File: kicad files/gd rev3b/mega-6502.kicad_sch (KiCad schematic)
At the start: 63 parts, among them J1 XY, Q1 BC817, SW1 MEGA RESET, U1 Apple_MEGA_II, U10 DRAM64KX4, U2 w65c02s, U3 74LVC1G02, U35 74LVC2G04, U4 74HC245, U5 74HC245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

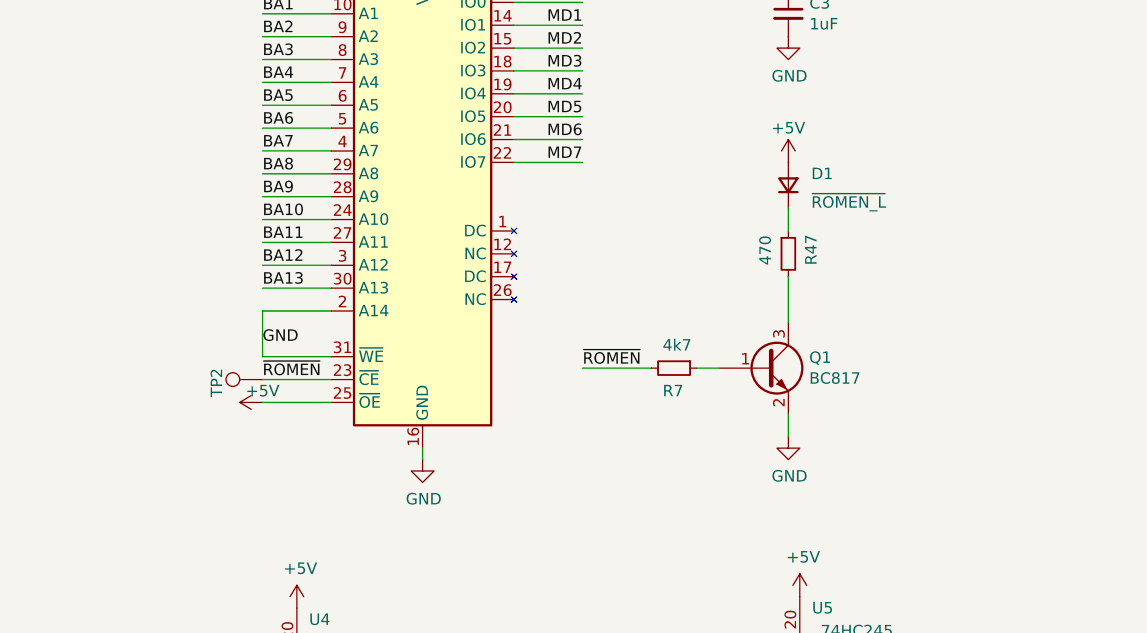
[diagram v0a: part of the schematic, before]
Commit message: Schematic changes for #52, #50, #70, #51, #61, #69, #71
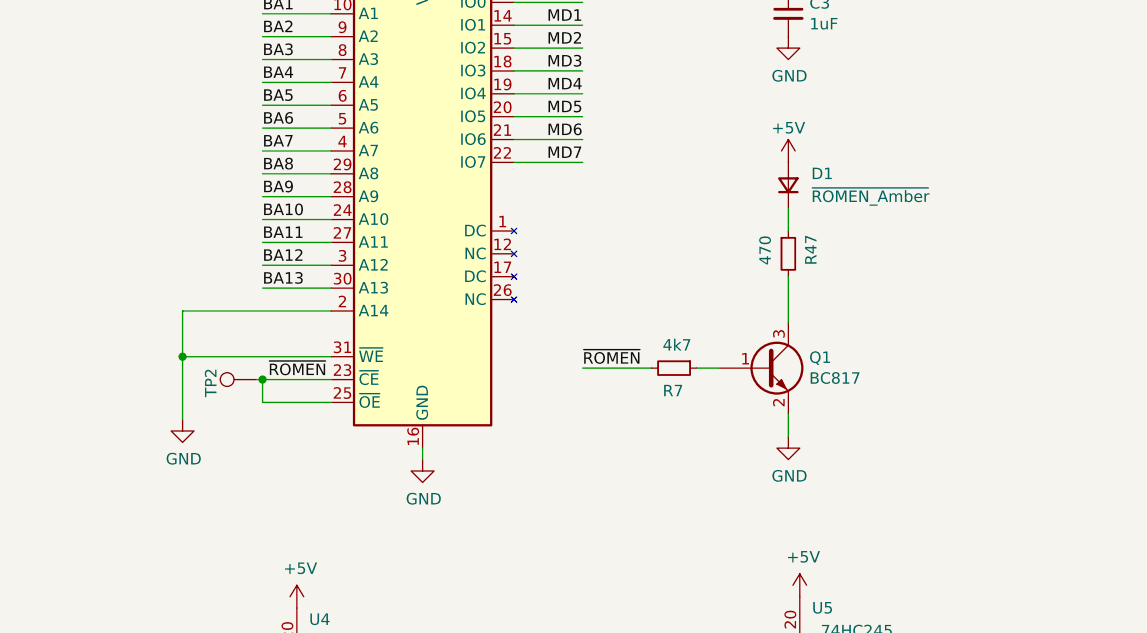
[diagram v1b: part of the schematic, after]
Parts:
- D1: value ~{ROMEN_L} -> ~{ROMEN_Amber}
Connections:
- net +5V: no longer U6.25 (~{OE})
- net ~{ROMEN}: now also U6.25 (~{OE})
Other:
- moved on the sheet: TP2
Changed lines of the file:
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@@
     (company "twitch.tv/baldengineer")
   )
+  (junction (at 214.63 187.96) (diameter 0) (color 0 0 0 0)
+  )
   (junction (at 350.52 194.31) (diameter 0) (color 0 0 0 0)
   )
@@
   (junction (at 127 187.96) (diameter 0) (color 0 0 0 0)
   )
+  (junction (at 205.74 185.42) (diameter 0) (color 0 0 0 0)
+  )
   (junction (at 127 264.16) (diameter 0) (color 0 0 0 0)
   )
@@
     (stroke (width 0) (type default))
   )
+  (wire (pts (xy 214.63 187.96) (xy 214.63 190.5))
+    (stroke (width 0) (type default))
+  )
   (wire (pts (xy 137.16 228.6) (xy 147.32 228.6))
     (stroke (width 0) (type default))
@@
     (stroke (width 0) (type default))
   )
+  (wire (pts (xy 214.63 187.96) (xy 213.995 187.96))
+    (stroke (width 0) (type default))
+  )
   (wire (pts (xy 242.57 161.29) (xy 250.19 161.29))
     (stroke (width 0) (type default))
@@
     (stroke (width 0) (type default))
   )
+  (wire (pts (xy 205.74 180.34) (xy 205.74 185.42))
+    (stroke (width 0) (type default))
+  )
   (wire (pts (xy 109.22 53.34) (xy 104.14 53.34))
     (stroke (width 0) (type default))
@@
     (stroke (width 0) (type default))
   )
+  (wire (pts (xy 205.74 185.42) (xy 205.74 192.405))
+    (stroke (width 0) (type default))
+  )
   (wire (pts (xy 347.98 148.59) (xy 347.98 149.86))
     (stroke (width 0) (type default))
@@
     (stroke (width 0) (type default))
   )
-  (wire (pts (xy 214.63 180.34) (xy 222.25 180.34))
+  (wire (pts (xy 205.74 180.34) (xy 222.25 180.34))
     (stroke (width 0) (type default))
   )
@@
     (stroke (width 0) (type default))
   )
-  (wire (pts (xy 222.25 185.42) (xy 214.63 185.42))
+  (wire (pts (xy 222.25 185.42) (xy 205.74 185.42))
     (stroke (width 0) (type default))
   )
@@
     (stroke (width 0) (type default))
   )
-  (wire (pts (xy 214.63 180.34) (xy 214.63 185.42))
-    (stroke (width 0) (type default))
-  )
   (wire (pts (xy 318.77 100.33) (xy 325.12 100.33))
     (stroke (width 0) (type default))
@@
     (effects (font (size 1.27 1.27)) (justify left bottom))
   )
-  (label "~{ROMEN}" (at 214.63 187.96 0) (fields_autoplaced)
+  (label "~{ROMEN}" (at 215.265 187.96 0) (fields_autoplaced)
     (effects (font (size 1.27 1.27)) (justify left bottom))
   )
@@
     (effects (font (size 1.27 1.27)) (justify right bottom))
   )
-  (label "GND" (at 214.63 184.15 0) (fields_autoplaced)
-    (effects (font (size 1.27 1.27)) (justify left bottom))
-  )
   (label "~{DMA}" (at 158.75 111.76 180) (fields_autoplaced)
     (effects (font (size 1.27 1.27)) (justify right bottom))
@@
     (effects (font (size 1.27 1.27)) (justify right))
   )
+  (symbol (lib_id "power:GND") (at 205.74 192.405 0) (unit 1)
+    (in_bom yes) (on_board yes) (dnp no)
+    (property "Reference" "#PWR022" (at 205.74 198.755 0)
+      (effects (font (size 1.27 1.27)) hide)
+    )
+    (property "Value" "GND" (at 205.867 196.7992 0)
+      (effects (font (size 1.27 1.27)))
+    )
+    (property "Footprint" "" (at 205.74 192.405 0)
+      (effects (font (size 1.27 1.27)) hide)
+    )
+    (property "Datasheet" "" (at 205.74 192.405 0)
+      (effects (font (size 1.27 1.27)) hide)
+    )
+    (pin "1")
+    (instances
+      (project "gd rev3b"
+        (path "/e63e39d7-6ac0-4ffd-8aa3-1841a4541b55/1d17904d-638f-48f3-894f-0144911f4a7c"
+          (reference "#PWR022") (unit 1)
+        )
+      )
+    )
+  )
   (symbol (lib_id "Mega IIe Rev3 Symbols:C_Small") (at 389.89 229.87 0) (unit 1)
     (in_bom yes) (on_board yes) (dnp no)
@@
     )
   )
-  (symbol (lib_name "TestPoint_Harwin_1") (lib_id "Mega IIe Rev3 Symbols:TestPoint_Harwin_1") (at 214.63 187.96 90) (unit 1)
+  (symbol (lib_name "TestPoint_Harwin_1") (lib_id "Mega IIe Rev3 Symbols:TestPoint_Harwin_1") (at 213.995 187.96 90) (unit 1)
     (in_bom yes) (on_board yes) (dnp no)
-    (property "Reference" "TP2" (at 209.55 186.69 0)
+    (property "Reference" "TP2" (at 208.915 186.69 0)
       (effects (font (size 1.27 1.27)) (justify right))
     )
-    (property "Value" "TestPoint_Harwin" (at 213.9442 186.4868 0)
+    (property "Value" "TestPoint_Harwin" (at 213.3092 186.4868 0)
       (effects (font (size 1.27 1.27)) (justify left) hide)
     )
-    (property "Footprint" "TestPoint:TestPoint_Pad_D1.0mm" (at 214.63 182.88 0)
+    (property "Footprint" "TestPoint:TestPoint_Pad_D1.0mm" (at 213.995 182.88 0)
       (effects (font (size 1.27 1.27)) hide)
     )
-    (property "Datasheet" "~" (at 214.63 182.88 0)
+    (property "Datasheet" "~" (at 213.995 182.88 0)
       (effects (font (size 1.27 1.27)) hide)
     )
@@
     )
   )
-  (symbol (lib_id "power:+5V") (at 214.63 190.5 90) (unit 1)
-    (in_bom yes) (on_board yes) (dnp no)
-    (property "Reference" "#PWR0104" (at 218.44 190.5 0)
-      (effects (font (size 1.27 1.27)) hide)
-    )
-    (property "Value" "+5V" (at 214.63 189.23 90)
-      (effects (font (size 1.27 1.27)))
-    )
-    (property "Footprint" "" (at 214.63 190.5 0)
-      (effects (font (size 1.27 1.27)) hide)
-    )
-    (property "Datasheet" "" (at 214.63 190.5 0)
-      (effects (font (size 1.27 1.27)) hide)
-    )
-    (pin "1")
-    (instances
-      (project "gd rev3b"
-        (path "/e63e39d7-6ac0-4ffd-8aa3-1841a4541b55/1d17904d-638f-48f3-894f-0144911f4a7c"
-          (reference "#PWR0104") (unit 1)
-        )
-      )
-    )
-  )
   (symbol (lib_id "Mega IIe Rev3 Symbols:C_Small") (at 374.65 172.72 0) (unit 1)
     (in_bom yes) (on_board yes) (dnp no)
@@
   (symbol (lib_id "Mega IIe Rev3 Symbols:D_1206") (at 273.05 166.37 90) (unit 1)
     (in_bom yes) (on_board yes) (dnp no) (fields_autoplaced)
-    (property "Reference" "D1" (at 275.59 165.0999 90)
+    (property "Reference" "D1" (at 275.59 165.1 90)
       (effects (font (size 1.27 1.27)) (justify right))
     )
-    (property "Value" "~{ROMEN_L}" (at 275.59 168.2749 90)
+    (property "Value" "~{ROMEN_Amber}" (at 275.59 167.64 90)
       (effects (font (size 1.27 1.27)) (justify right))
     )
